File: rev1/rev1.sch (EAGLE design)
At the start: 38 parts, among them Q1 MOSFET-NCHANNEL-IRLR3705ZPBF, Q2 MOSFET-PCHANNEL, Q3 MOSFET-NCHANNELBSS138, U1 ATMEGA168-AU, U2 5v, U3 74AHC1G04DBV, Y1 16MHz

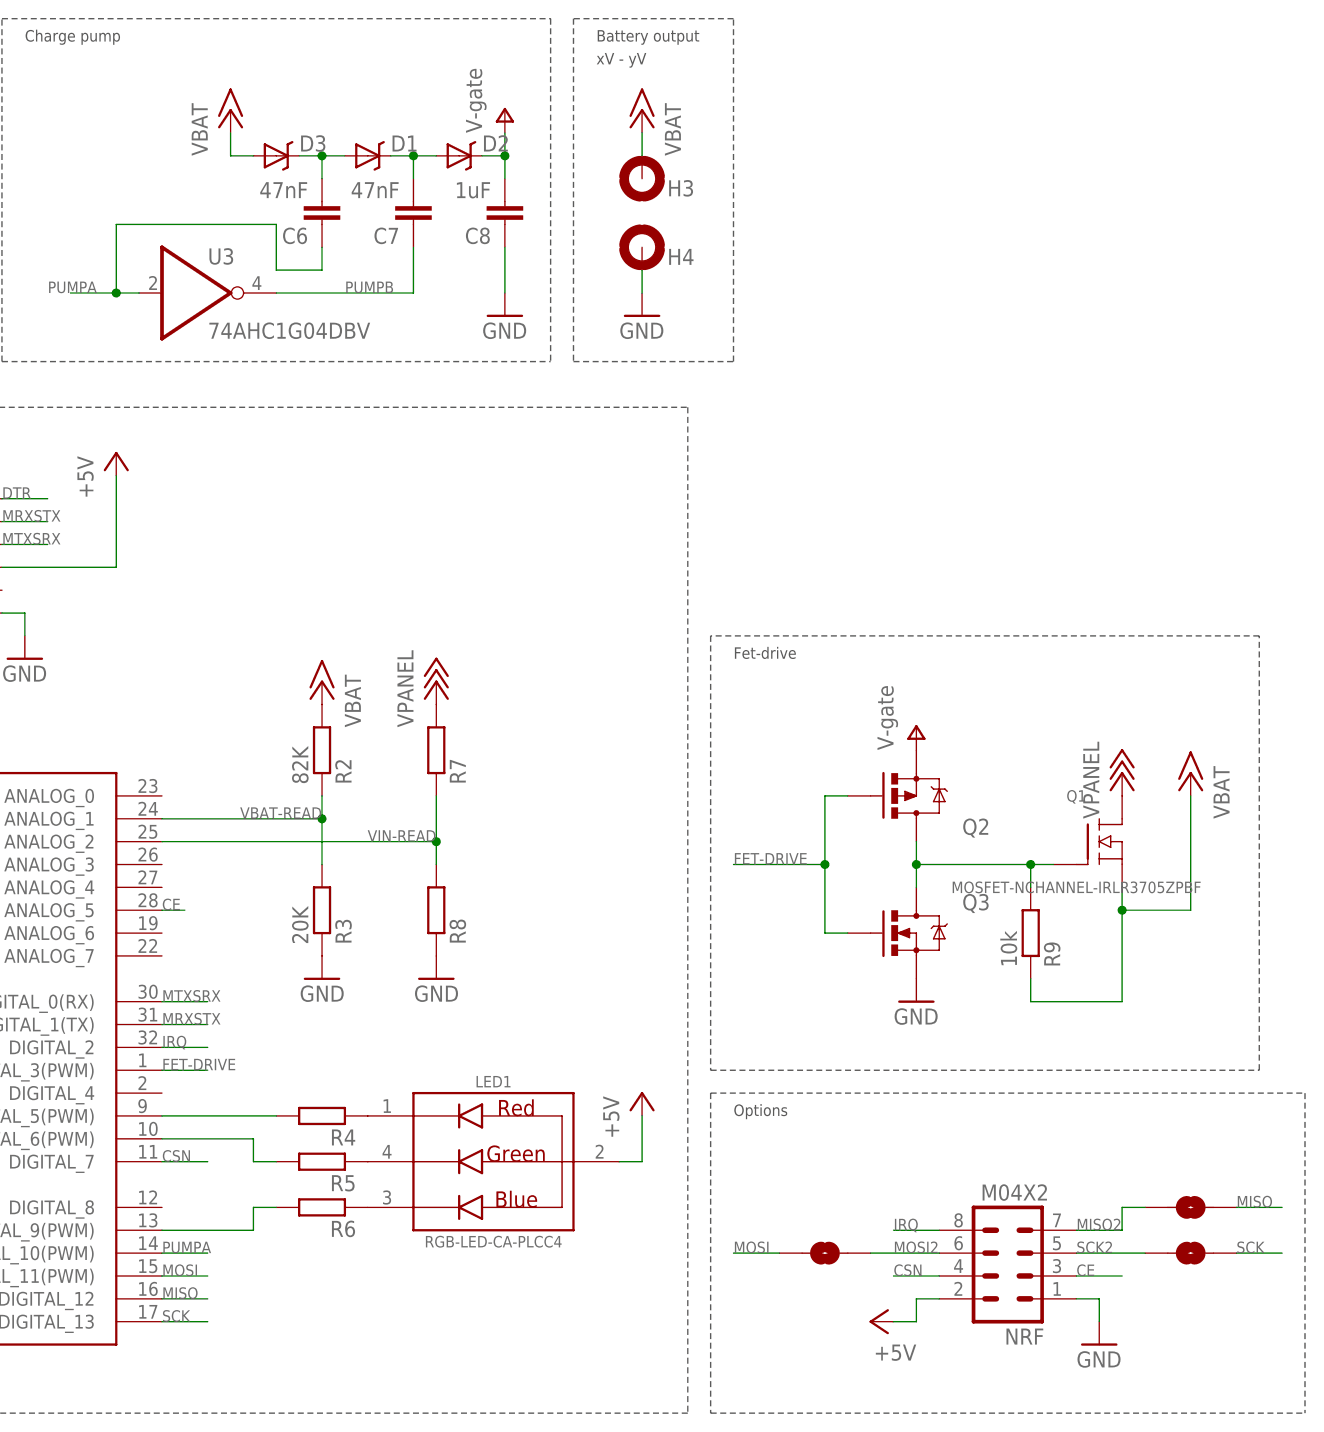
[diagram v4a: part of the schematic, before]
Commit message: Added copper pour, sorted silk screen
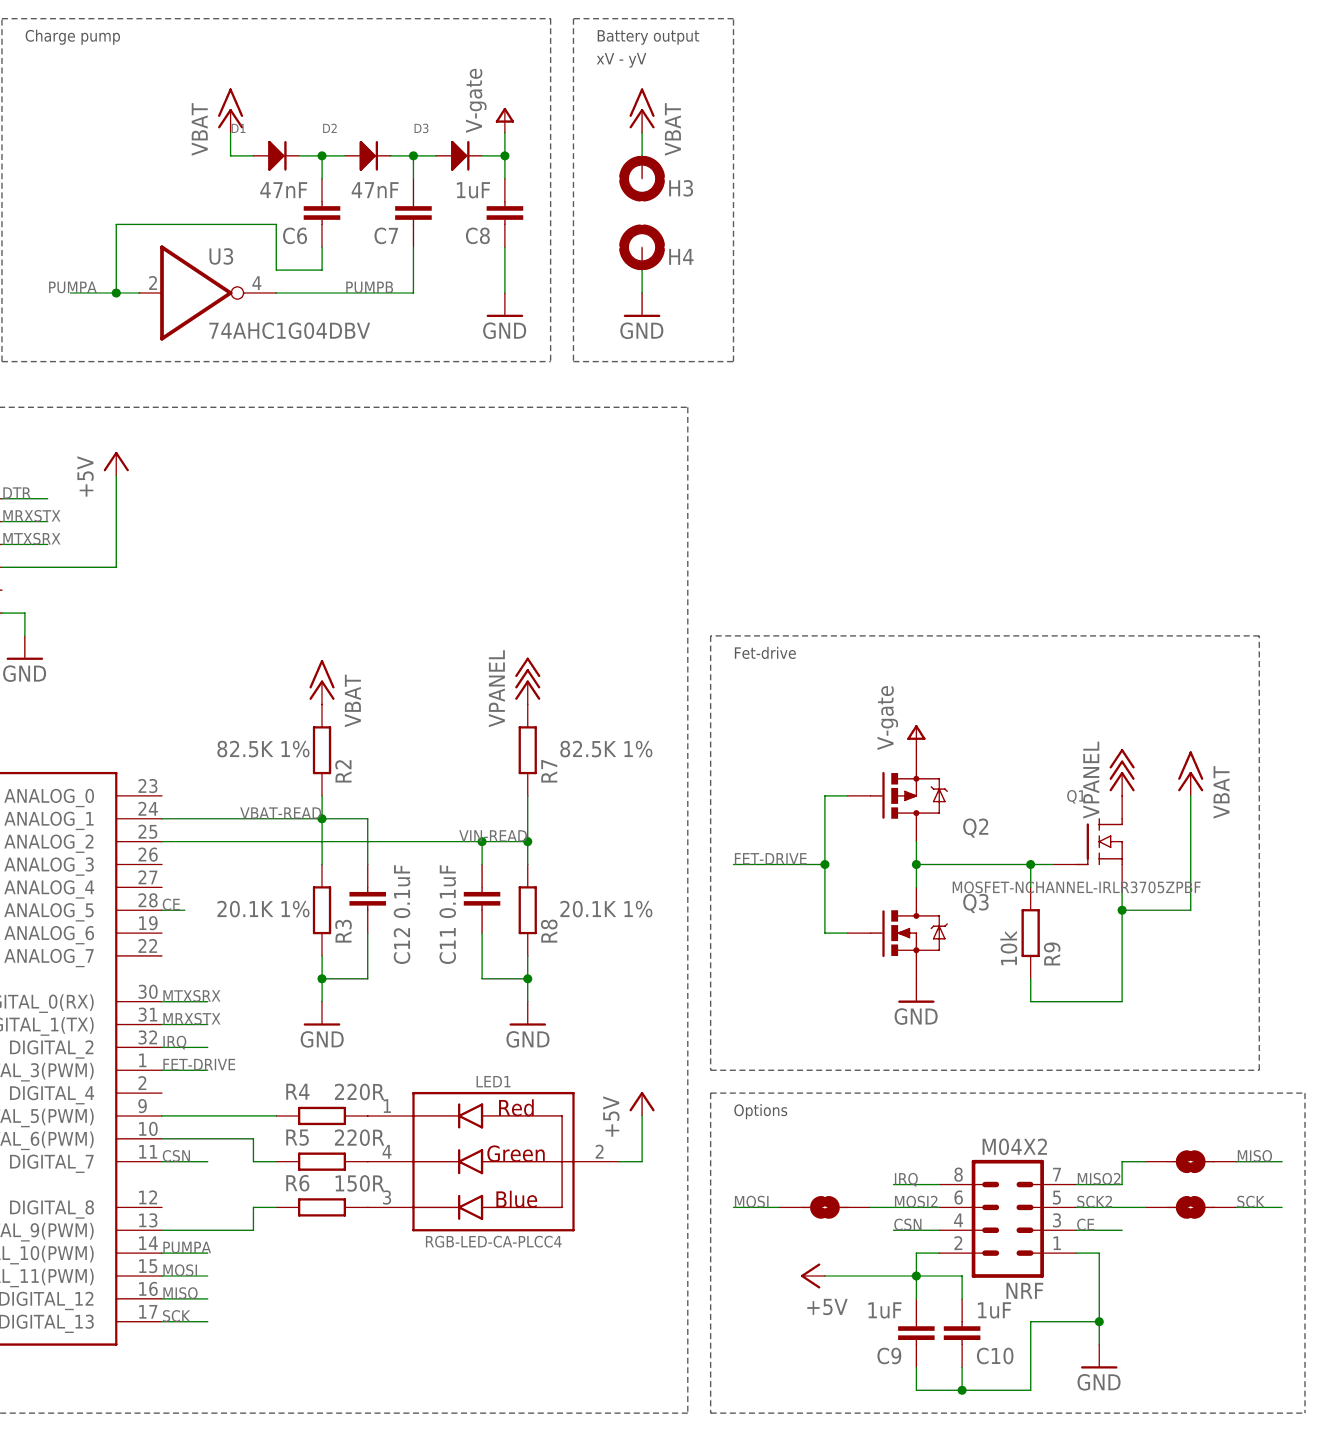
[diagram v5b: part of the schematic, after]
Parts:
- added C10, C9: 1uF, resistor:C-EUC0603K
- added C11, C12: 0.1uF, resistor:C-EUC0603K
- D1, D2, D3: value DIODE-SCHOTTKY -> (none); device SparkFun-DiscreteSemi:DIODE-SCHOTTKY -> MF_Discrete_Semiconductor:DIODE_SOD-123
- R2: value 82K -> 82.5K 1%
- R3: value 20K -> 20.1K 1%
- R4, R5: value (none) -> 220R
- R6: value (none) -> 150R
- R7: value (none) -> 82.5K 1%
- R8: value (none) -> 20.1K 1%
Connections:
- net +15V: now also D1.ANODE; no longer D3.A
- net +5V: now also C10.2, C9.2
- net GND: now also C10.1, C11.1, C12.1, C9.1
- net N$10: now also D1.CATHODE, D2.ANODE; no longer D1.A, D3.C
- net N$8: now also D2.CATHODE, D3.ANODE; no longer D1.C, D2.A
- net V+: now also D3.CATHODE; no longer D2.C
- net VBAT-READ: now also C12.2
- net VIN-READ: now also C11.2
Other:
- moved on the sheet: NRF, R7, R8
